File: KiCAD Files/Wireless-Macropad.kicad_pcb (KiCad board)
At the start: 2 copper layers, 109.2 x 86.1 mm, 22 parts, among them SW1 RotaryEncoder_Switch, SW10 SW_SPDT, SW2 SW_Push, SW3 SW_Push, SW4 SW_Push, SW5 SW_Push, SW6 SW_Push, SW7 SW_Push, SW8 SW_Push, SW9 SW_Push, U1 106990290

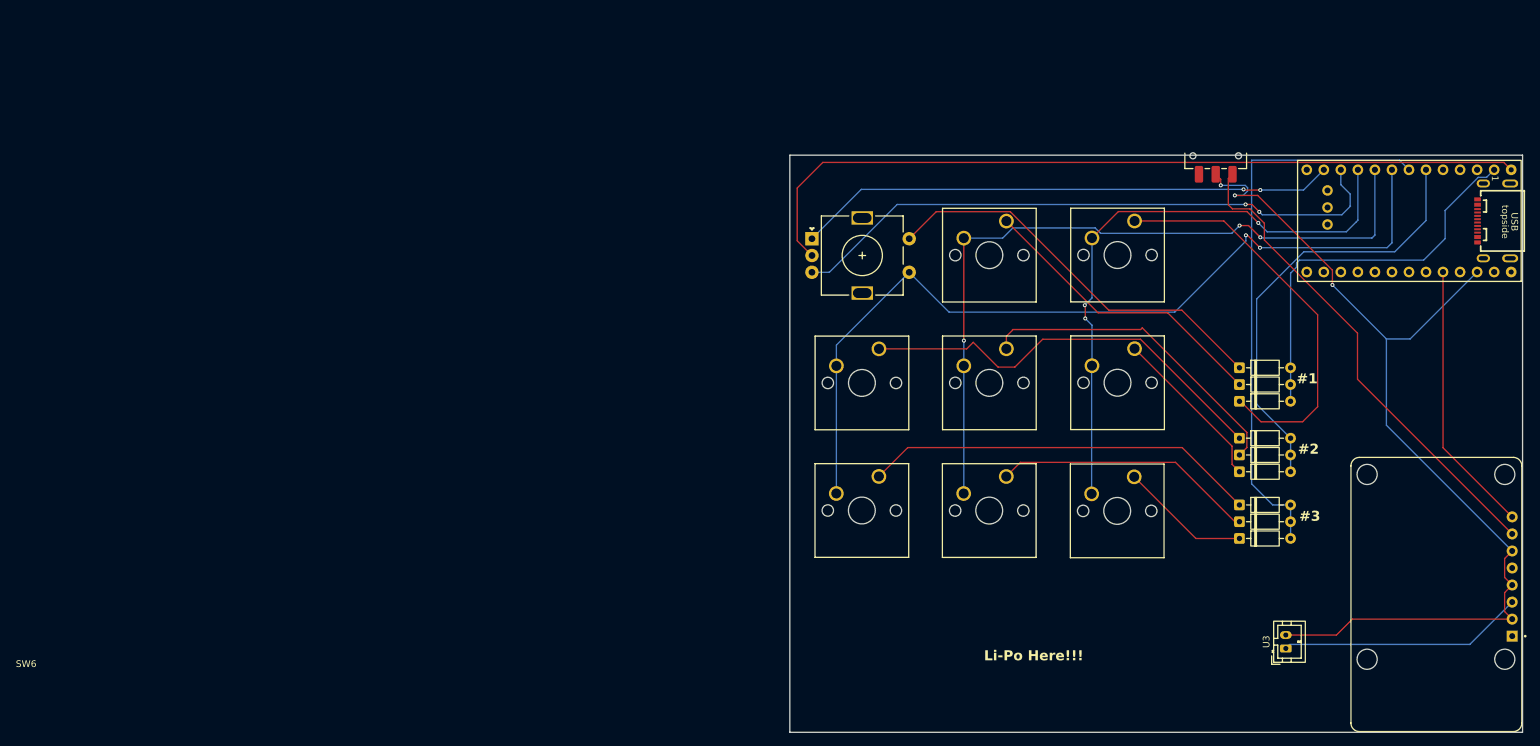
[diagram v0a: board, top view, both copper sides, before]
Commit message: Updated my PCB and generated my gerber file
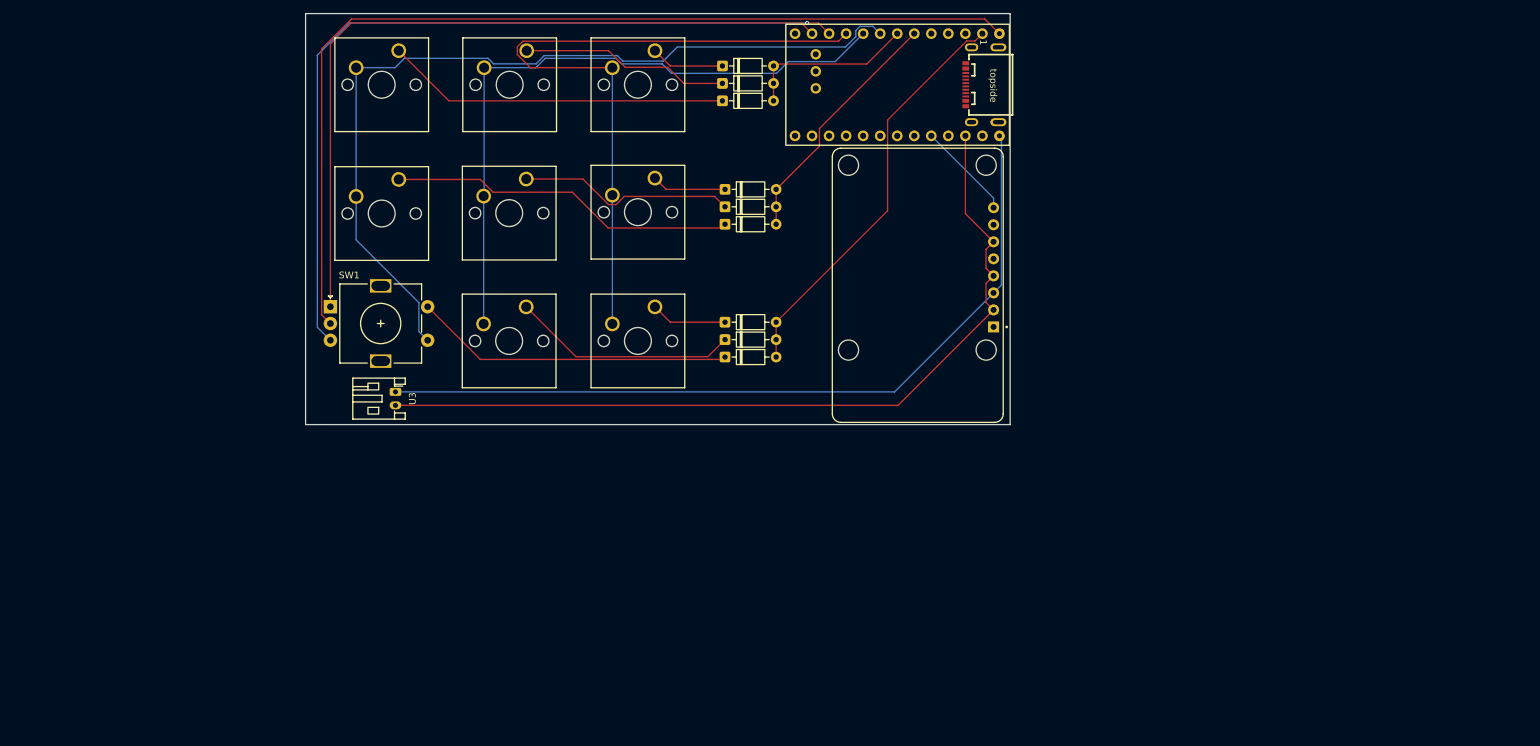
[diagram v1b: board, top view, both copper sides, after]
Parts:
- removed SW10: SW_SPDT, Button_Switch_SMD:SW_SPDT_CK_JS102011SAQN
- U3: footprint Connector_JST:JST_PH_B2B-PH-K_1x02_P2.00mm_Vertical -> Connector_JST:JST_PH_S2B-PH-K_1x02_P2.00mm_Horizontal
- moved U3 138.2 mm to (67.7, 95.4), turned to -90 degrees
- moved D8 104.4 mm to (116.4, 46.8)
- moved D7 101.1 mm to (116.4, 49.4)
- moved D4 97.8 mm to (116.4, 52.0)
- moved SW7 95.7 mm to (68.1, 44.5)
- moved SW9 95.6 mm to (106.3, 44.5)
- moved SW8 95.6 mm to (87.2, 44.5)
- moved U1 90.0 mm to (145.5, 79.5)
- moved D9 87.5 mm to (116.8, 65.2)
- moved D6 85.2 mm to (116.8, 67.8)
- moved D3 83.1 mm to (116.8, 70.4)
- moved U2 79.0 mm to (157.7, 42.0)
- moved D10 77.6 mm to (116.8, 85.0)
- moved D5 77.0 mm to (116.8, 87.6)
- moved D2 76.7 mm to (116.8, 90.2)
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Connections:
- U1 pad 7: Net-(SW10-A) -> unconnected-(U1-EN-Pad7)
- U2 pad 29: unconnected-(U2-BAT-Pad29) -> Net-(U1-BAT)
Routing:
- net Net-(U1-BAT): track 36.6 -> 119.3 mm
- net Net-(SW10-A): track 72.9 -> 0.00 mm
- net Row 3: track 84.4 -> 25.6 mm
- net Net-(D10-K): track 60.7 -> 11.4 mm
- net Net-(U2-D8): track 80.7 -> 113.0 mm, vias 2 -> 0
- net Net-(U2-D7): track 91.7 -> 122.3 mm, vias 2 -> 1
- net Row 2: track 65.5 -> 37.0 mm
- net Net-(U1-3V3): track 40.8 -> 14.6 mm
- net Net-(SW1-PadC): track 119.5 -> 145.3 mm
- net GND: track 145.3 -> 124.6 mm, vias 3 -> 0
- net Net-(D6-K): track 48.6 -> 32.4 mm
- net Column 3: track 89.8 -> 104.2 mm, vias 3 -> 0
- net Net-(D9-K): track 24.8 -> 11.1 mm
- net Net-(D2-K): track 60.5 -> 47.7 mm
- net Column 2: track 111.5 -> 98.7 mm, vias 3 -> 0
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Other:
- board size 109.2 x 86.1 mm -> 105.1 x 61.3 mm
- board text removed: "#1"
- board text removed: "#2"
- board text removed: "#3"
- board text removed: "Li-Po Here!!!"
